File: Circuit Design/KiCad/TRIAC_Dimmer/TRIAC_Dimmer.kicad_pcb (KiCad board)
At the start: 2 copper layers, 17 parts, among them J1 1726480102, J2 1726480102, Q1 BT136-600

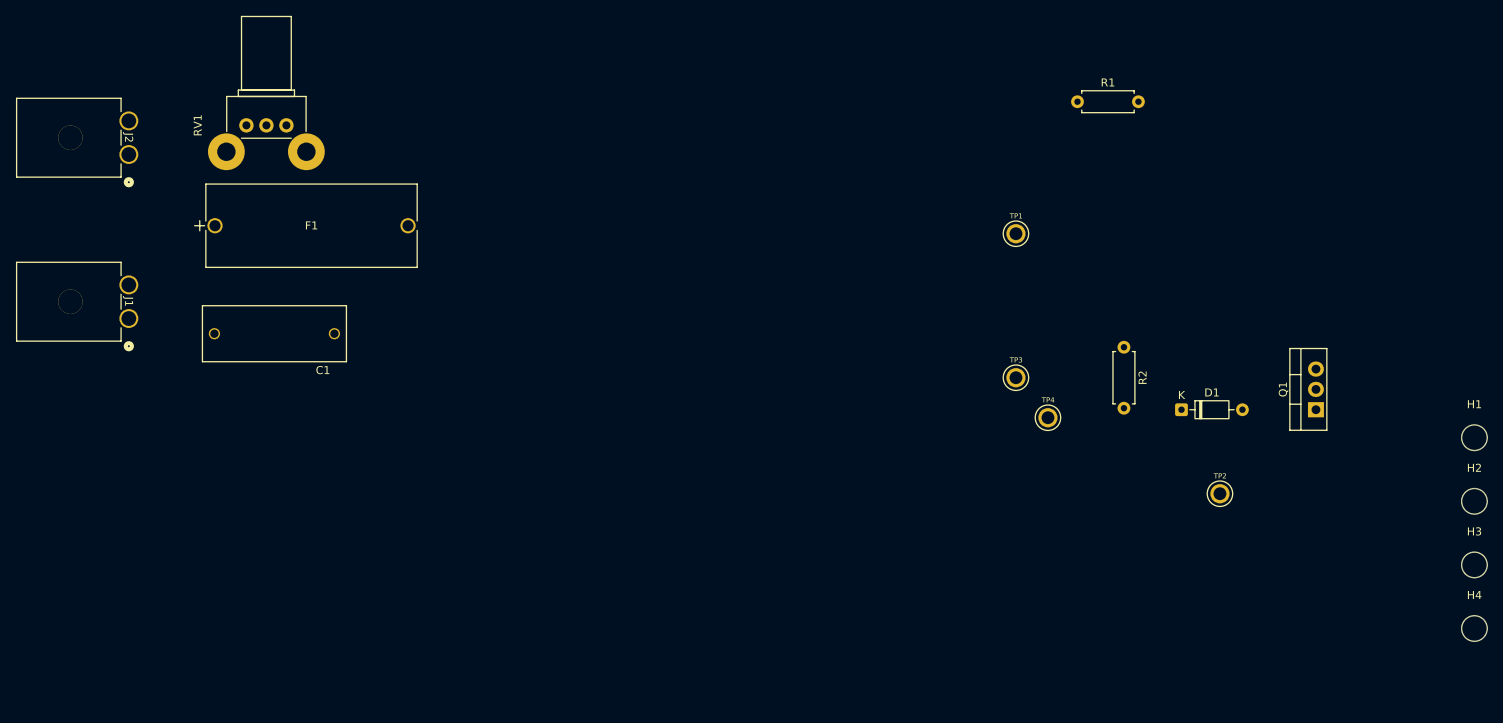
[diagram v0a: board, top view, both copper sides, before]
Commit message: PCB libraries were global, made them local
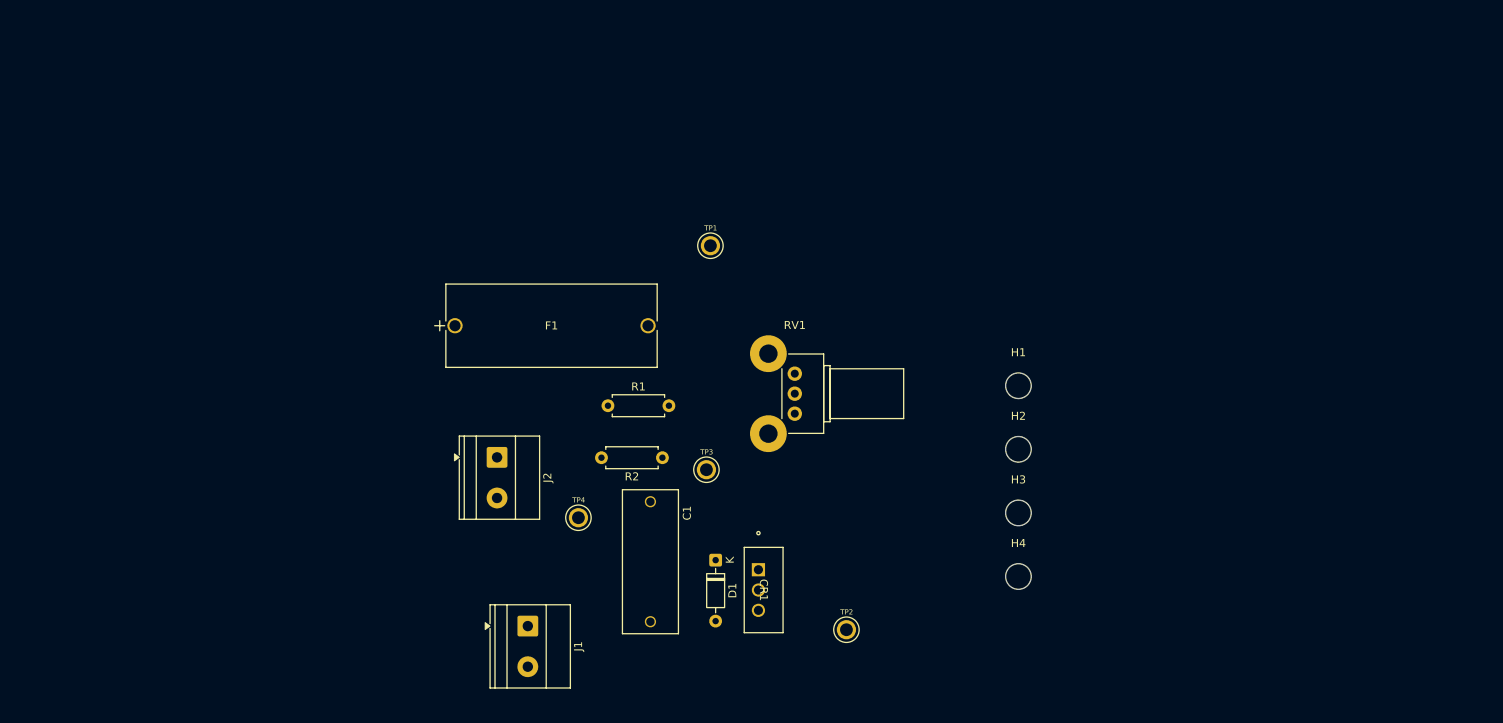
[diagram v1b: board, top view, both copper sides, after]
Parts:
- removed Q1: BT136-600, Package_TO_SOT_THT:TO-220-3_Vertical
- added CR1: BTB04-600SL, TO-220AB_STM:TO-220AB_STM, F.Cu at (151.0, 90.5)
- C1: value B32672L6104K000 -> 0.1uF; footprint Personal_Capacitor_THT:CAPRR1500W80L1800T700H1250 -> CAPRR1500W80L1800T700H1250:CAPRR1500W80L1800T700H1250
- F1: footprint Personal_Fuses:FUSE_05200101Z_LTF -> FUSE_05200101Z_LTF:FUSE_05200101Z_LTF
- J1, J2: value 1726480102 -> Screw_Terminal_01x02; footprint Personal_Connector_THT:CONN_SD-172648-0000_02_MOL -> TerminalBlock_Phoenix:TerminalBlock_Phoenix_MKDS-1,5-2-5.08_1x02_P5.08mm_Horizontal
- TP1, TP2, TP3, TP4: footprint Personal_Test_Point_THT:KEYSTONE_5271 -> KEYSTONE_5271:KEYSTONE_5271
- moved RV1 73.1 mm to (155.5, 71.0), turned to 0 degrees
- moved R1 69.9 mm to (132.2, 70.0)
- moved J1 63.0 mm to (122.2, 97.5)
- moved D1 61.2 mm to (145.7, 89.3), turned to -90 degrees
- moved TP4 60.0 mm to (128.5, 84.0)
- moved J2 59.6 mm to (118.3, 76.5)
- moved R2 59.3 mm to (139.0, 76.5), turned to 180 degrees
- moved H1 57.4 mm to (183.5, 67.5)
- moved H2 57.4 mm to (183.5, 75.5)
- moved H3 57.4 mm to (183.5, 83.4)
- moved H4 57.4 mm to (183.5, 91.3)
- moved C1 55.0 mm to (137.5, 89.5), turned to -90 degrees
- moved TP2 49.7 mm to (162.0, 98.0)
- moved TP3 40.4 mm to (144.5, 78.0)
- moved TP1 38.2 mm to (145.0, 50.0)
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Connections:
- C1 pad 2: Net-(Q1-A1) -> Net-(J1-Pin_2)
- F1 pad 1: Net-(F1-Pad1) -> Net-(J2-Pin_1)
- J1 pad 1: Net-(Q1-A1) -> Net-(J1-Pin_1)
- J1 pad 2: Net-(J1-Pad2) -> Net-(J1-Pin_2)
- J2 pad 1: Net-(J1-Pad2) -> Net-(J2-Pin_1)
- J2 pad 2: Net-(F1-Pad1) -> Net-(J1-Pin_1)
- TP2 pad 1: Net-(Q1-A1) -> Net-(J1-Pin_2)

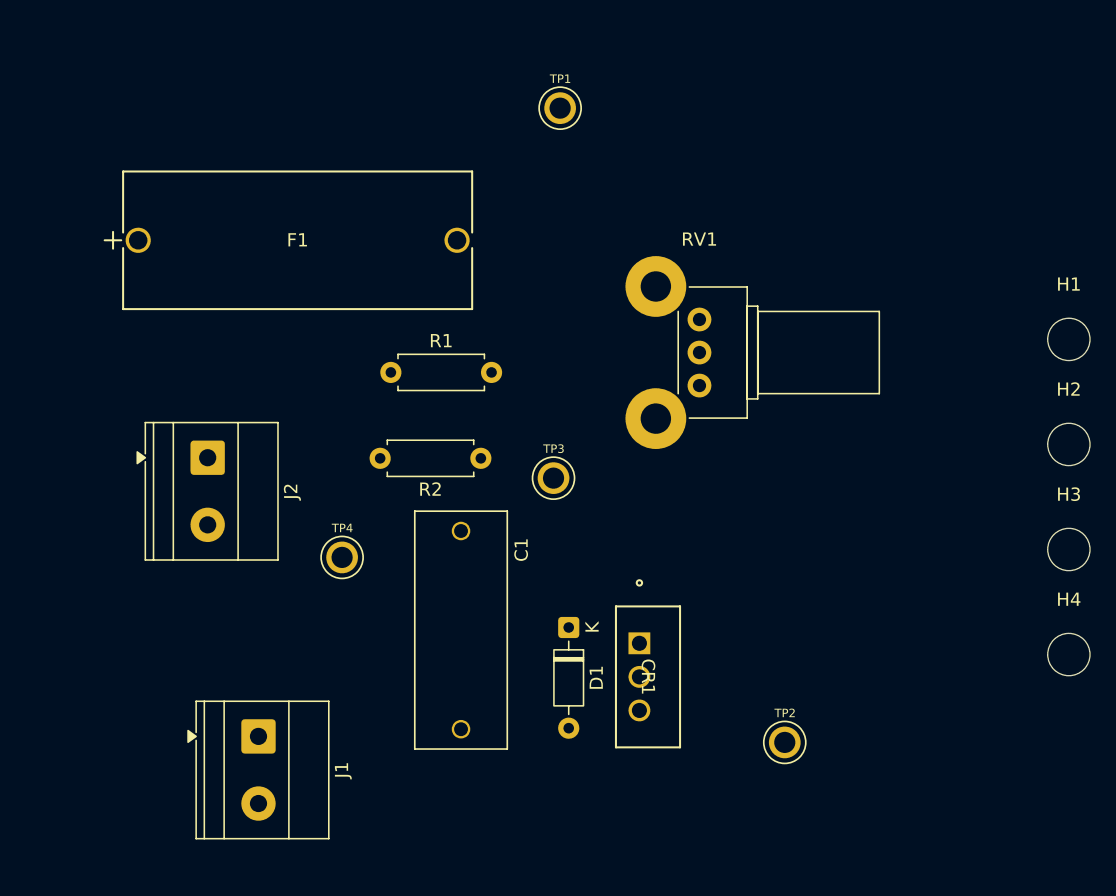
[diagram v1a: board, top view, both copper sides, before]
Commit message: Rough layout complete
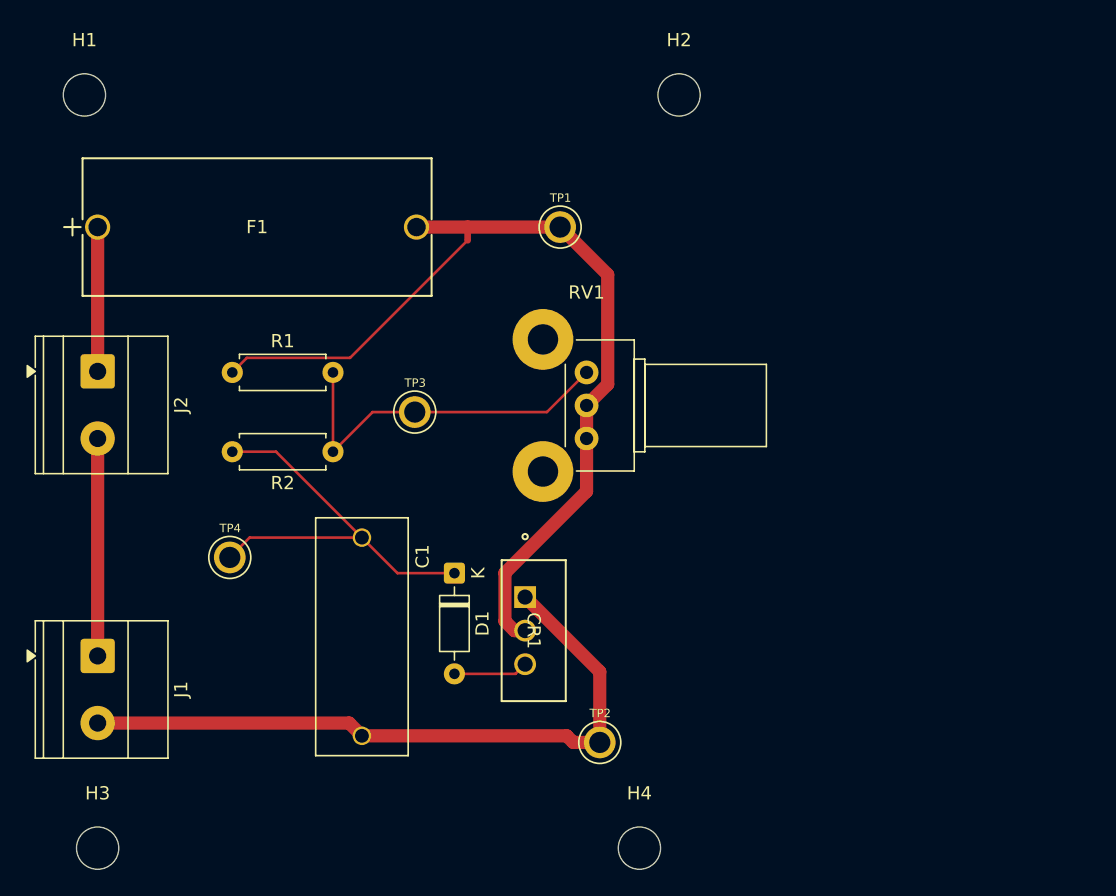
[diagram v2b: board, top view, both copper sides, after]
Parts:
- added NT1: NetTie_2, NetTie:NetTie-2_SMD_Pad0.5mm, F.Cu at (138.0, 59.5)
- moved H3 76.9 mm to (110.0, 106.0)
- moved H1 76.8 mm to (109.0, 49.0)
- moved H2 39.6 mm to (154.0, 49.0)
- moved H4 35.6 mm to (151.0, 106.0)
- moved TP2 14.0 mm to (148.0, 98.0)
- moved J1 13.6 mm to (110.0, 91.5)
- moved R1 12.0 mm to (120.2, 70.0)
- moved TP3 11.6 mm to (134.0, 73.0)
- moved R2 11.2 mm to (127.8, 76.0)
- moved J2 10.6 mm to (110.0, 69.9)
- moved D1 9.58 mm to (137.0, 85.2)
- moved RV1 9.44 mm to (147.0, 75.0)
- moved CR1 9.33 mm to (142.3, 87.0)
- moved TP1 9.00 mm to (145.0, 59.0)
- moved TP4 8.50 mm to (120.0, 84.0)
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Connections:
- R1 pad 1: Net-(CR1-Pad2) -> Net-(NT1-Pad1)
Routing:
- net Net-(J1-Pin_2): track 0.00 -> 51.9 mm
- net Net-(CR1-Pad2): track 0.00 -> 47.2 mm
- net Net-(D1-K): track 0.00 -> 31.2 mm
- net Net-(R1-Pad2): track 0.00 -> 27.7 mm
- net Net-(NT1-Pad1): track 0.00 -> 22.0 mm
- net Net-(J1-Pin_1): track 0.00 -> 16.5 mm
- net Net-(J2-Pin_1): track 0.00 -> 10.9 mm
- net Net-(D1-A): track 0.00 -> 5.65 mm
